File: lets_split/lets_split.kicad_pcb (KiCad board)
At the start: 2 copper layers, 112 x 79 mm, 62 parts, among them J1 3PIN, J2 6PIN, J3 3PIN, SW1 SW_PUSH, SW10 SW_PUSH, SW11 SW_PUSH, SW12 SW_PUSH, SW13 SW_PUSH, SW14 SW_PUSH, SW15 SW_PUSH, SW16 SW_PUSH, SW17 SW_PUSH, SW18 SW_PUSH, SW19 SW_PUSH, SW2 SW_PUSH, SW21 SW_PUSH, SW22 SW_PUSH, SW23 SW_PUSH, SW3 SW_PUSH, SW4 SW_PUSH, SW5 SW_PUSH, SW6 SW_PUSH, SW7 SW_PUSH, SW8 SW_PUSH, SW9 SW_PUSH, U2 HOLE, U3 HOLE, U4 HOLE, U5 HOLE

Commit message: added universal switch and stuff
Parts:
- removed ? (x2): SW_PUSH, flipalps:MXALPS_FLIP
- removed the G*** at (118.8, 78.0)
- removed the G*** at (127.0, 87.8)
- added G***: LOGO, Silks:AIRImicro, F.Cu at (141.0, 109.0)
- added G***: LOGO, Silks:BKB smaller chess, B.Cu at (62.0, 92.0)
- added G***: LOGO, Silks:Octopus1, F.Cu at (112.0, 92.0)
- added J10, J8, J9: Conn_01x01, BishopKicadConsolidated:PIN_1, F.Cu at (93.0, 122.1)
- added J11: Conn_01x01, BishopKicadConsolidated:PIN_1, F.Cu at (59.9, 35.7)
- added J12: Conn_01x01, BishopKicadConsolidated:PIN_1, F.Cu at (54.2, 51.0)
- added J4: Conn_01x01, BishopKicadConsolidated:PIN_1, F.Cu at (75.8, 37.9)
- added J5: Conn_01x01, BishopKicadConsolidated:PIN_1, F.Cu at (78.0, 37.9)
- added J6: Conn_01x01, BishopKicadConsolidated:PIN_1, F.Cu at (54.2, 53.6)
- added J7: Conn_01x01, BishopKicadConsolidated:PIN_1, F.Cu at (74.8, 48.4)
- added SW20: SW_PUSH, Universal-Switch-Footprint:MX-ALPs-PG1350-FLIP, F.Cu at (121.7, 104.0)
- added SW24: SW_PUSH, Universal-Switch-Footprint:MX-ALPs-PG1350-FLIP, F.Cu at (140.8, 104.0)
- added SW25: SW_PUSH, Universal-Switch-Footprint:MX-ALPs-PG1350-FLIP-2U, F.Cu at (131.2, 104.0)
- SW1, SW10, SW11, SW12, SW13, SW14, SW15, SW16, SW17, SW18, SW19, SW2, SW21, SW22, SW23, SW3, SW4, SW5, SW6, SW7, SW8, SW9: footprint flipalps:MXALPS_FLIP -> Universal-Switch-Footprint:MX-ALPs-PG1350-FLIP
- U1: value (none) -> TEENSY2.0
- moved D20 27.5 mm to (108.9, 94.5), turned to 180 degrees
- moved D5 18.9 mm to (69.7, 56.2)
- moved W1 12.1 mm to (131.2, 50.5)
- moved D21 11.3 mm to (147.2, 56.2), turned to 180 degrees
- moved D22 10.4 mm to (146.0, 75.4), turned to 180 degrees
- moved D23 10.3 mm to (147.3, 94.5), turned to 180 degrees
- moved D6 10.2 mm to (69.9, 75.4), turned to 180 degrees
- moved R1 9.85 mm to (93.1, 47.0), turned to 270 degrees
- moved R2 9.76 mm to (112.1, 47.0), turned to 90 degrees
- moved D17 8.66 mm to (125.4, 56.4), turned to 180 degrees
- moved D9 6.10 mm to (88.7, 56.4), turned to 180 degrees
- moved D13 5.63 mm to (108.3, 56.4), turned to 180 degrees
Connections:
- U1 pad 1: Net-(U1-Pad1) -> (no net)
- U1 pad 29: Net-(U1-Pad29) -> (no net)
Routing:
- net col5: track 133.7 -> 187.5 mm, vias 0 -> 1
- net VCC: track 27.2 -> 76.9 mm
- net col3: track 85.0 -> 123.0 mm, vias 0 -> 1
- net col2: track 68.2 -> 104.0 mm, vias 0 -> 1
- net col1: track 68.7 -> 99.0 mm
- net col4: track 112.3 -> 141.2 mm, vias 0 -> 1
- net data: track 117.5 -> 91.3 mm
- net GND: track 15.8 -> 42.0 mm, vias 0 -> 1
- net col0: track 96.5 -> 116.7 mm
- net Net-(D20-Pad2): track 8.15 -> 24.5 mm
- net Net-(D18-Pad2): track 6.11 -> 21.6 mm
- net xtradata: track 25.8 -> 10.8 mm
- net row3: track 143.1 -> 129.3 mm
- net Net-(D14-Pad2): track 6.62 -> 20.2 mm
- net Net-(D15-Pad2): track 6.65 -> 20.0 mm
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- added copper zone on B.Cu, net GND
- removed copper zone on B.Cu, net VCC
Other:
- outline, holes or cut-outs redrawn
- board text added: "Origonal design by Wootpatoot Update by Bishop Keyboards"
- board text added: "The standard English plural of octopus is octopuses."
- board text removed: "By Wootpatoot"

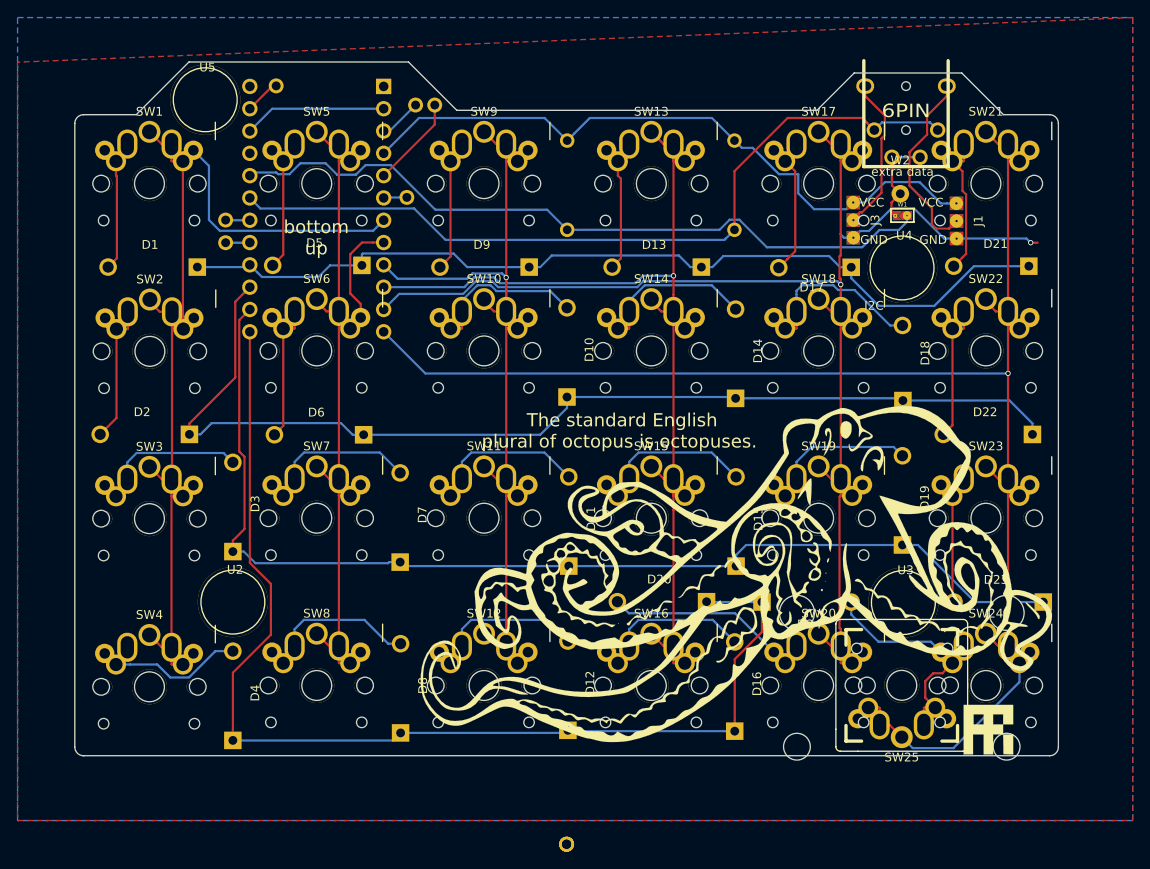
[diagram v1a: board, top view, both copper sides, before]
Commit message: fixed diodes broke traces
updated the diode footprint will have to fix traces now that the width of the diode pole spaces are different.
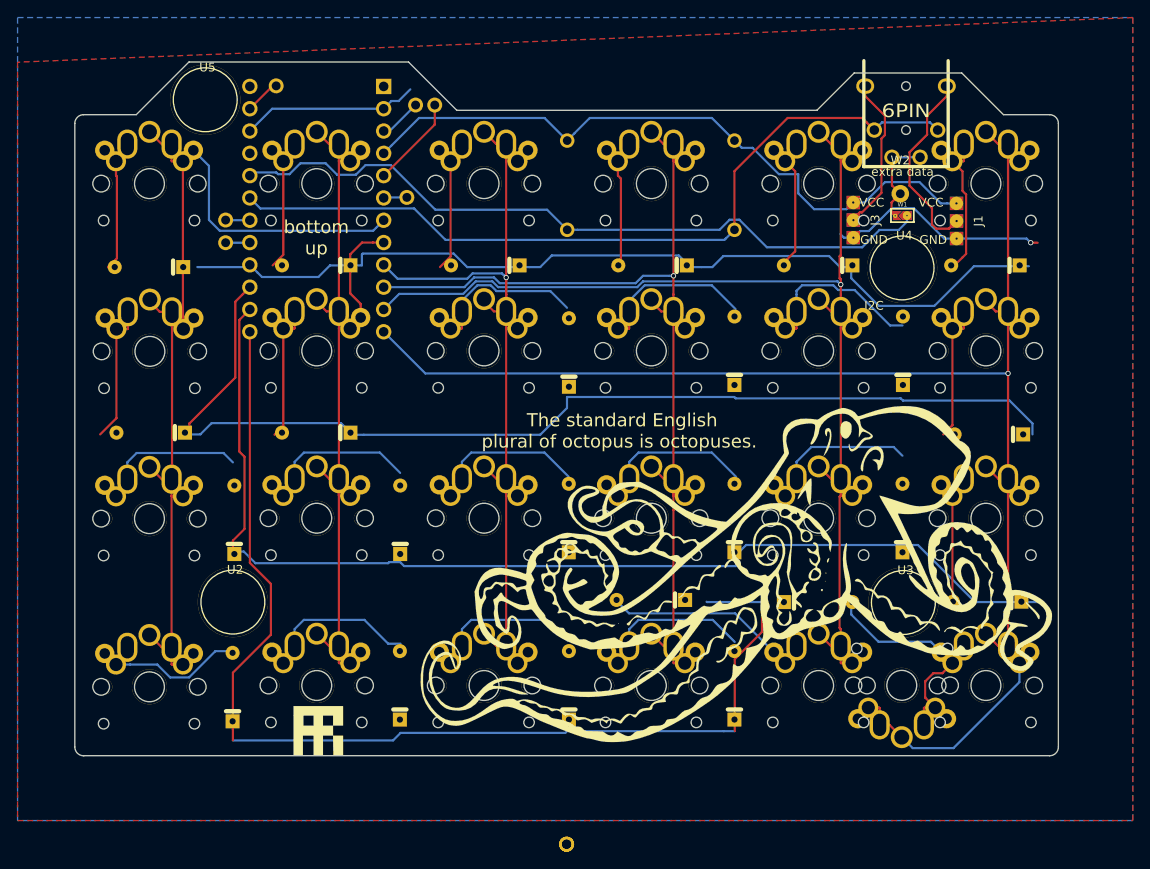
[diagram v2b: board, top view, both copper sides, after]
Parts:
- D1, D10, D11, D12, D13, D14, D15, D16, D17, D18, D19, D2, D20, D21, D22, D23, D24, D3, D4, D5, D6, D7, D8, D9: footprint Diodes_ThroughHole:Diode_DO-41_SOD81_Horizontal_RM10 -> BishopKicadConsolidated:D_axial_clean
- SW25: footprint Universal-Switch-Footprint:MX-ALPs-PG1350-FLIP-2U -> Universal-Switch-Footprint:MX-ALPs-PG1350-FLIP
- moved G*** 76.3 mm to (64.7, 109.1)
- moved D21 6.55 mm to (140.7, 56.2)
- moved D24 6.39 mm to (121.6, 94.5)
- moved D23 6.39 mm to (140.9, 94.5)
- moved D20 6.35 mm to (102.6, 94.3)
- moved D4 6.07 mm to (55.0, 104.2)
- moved D18 5.67 mm to (131.3, 65.9)
- moved D13 5.56 mm to (102.8, 56.2)
- moved D1 5.51 mm to (45.4, 56.4)
- moved D15 5.47 mm to (112.1, 84.9)
- moved D11 5.47 mm to (93.2, 84.9)
- moved D14 5.42 mm to (112.1, 65.9)
- moved D8 5.42 mm to (74.0, 104.0)
- moved D6 5.40 mm to (64.5, 75.2)
- moved D16 5.22 mm to (112.1, 104.0)
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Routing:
- net (no net): track 0.00 -> 279.6 mm
- net row1: track 121.7 -> 19.6 mm
- net row2: track 126.3 -> 28.9 mm
- net row0: track 104.4 -> 8.04 mm
- net Net-(D5-Pad2): track 16.6 -> 113.0 mm
- net row3: track 129.3 -> 49.3 mm
- net GND: track 42.0 -> 45.9 mm

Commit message: changed 3.5mm jack
updated 3.5mm jack to use the PJ320E
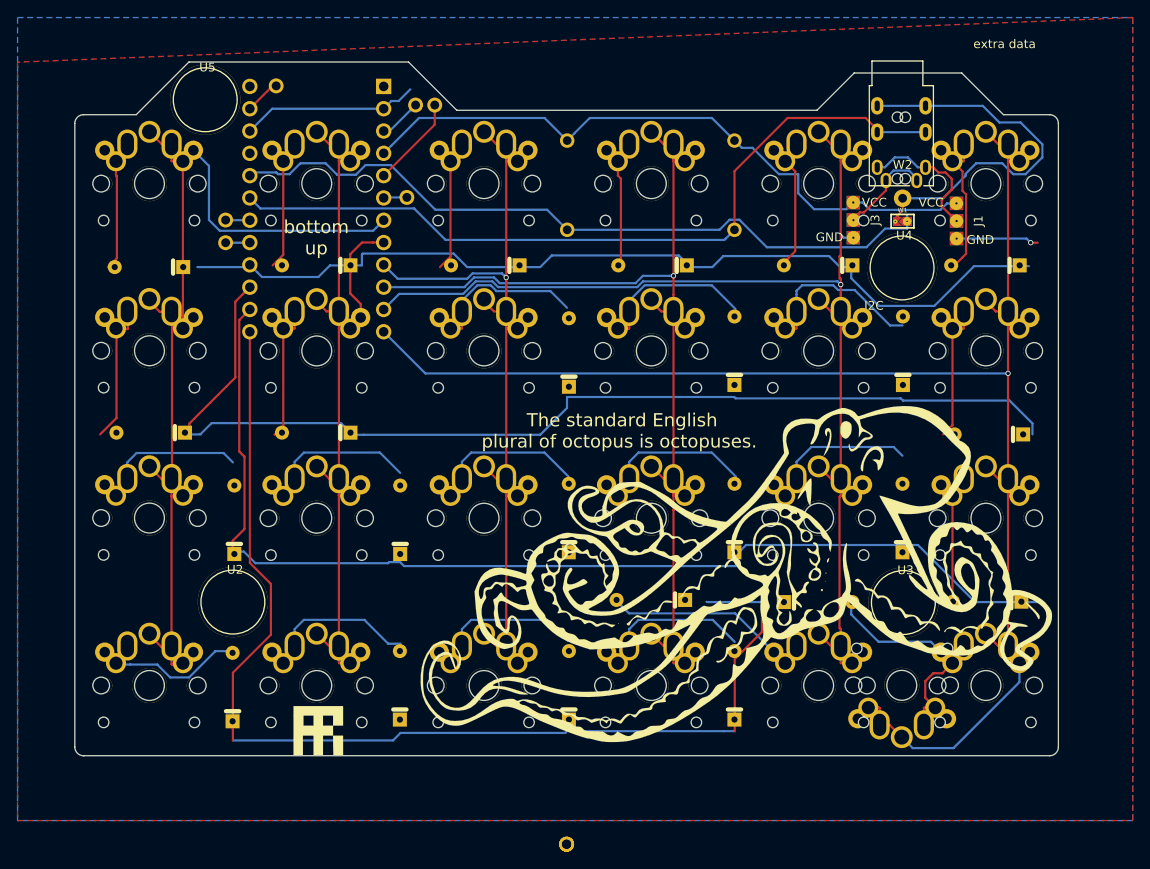
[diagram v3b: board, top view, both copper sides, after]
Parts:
- removed J2: 6PIN, footprint:4pin35mmAudio
- added TRRS1: 4pin 3.5mm, BishopKicadConsolidated:PJ320E_3.5mm_Jack_flip, F.Cu at (131.1, 39.3)
- moved W1 0.65 mm to (131.3, 51.1)
- moved W2 0.58 mm to (131.3, 48.5)
- moved SW4 0.15 mm to (45.5, 104.0)
- moved SW2 0.09 mm to (45.5, 65.9)
- moved SW3 0.07 mm to (45.5, 84.9)
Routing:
- net (no net): track 279.6 -> 64.0 mm
- net row1: track 19.6 -> 121.7 mm
- net row2: track 28.9 -> 126.3 mm
- net row0: track 8.04 -> 104.4 mm
- net Net-(D5-Pad2): track 113.0 -> 16.6 mm
- net xtradata: track 10.8 -> 44.8 mm
- net row3: track 49.3 -> 65.3 mm
- net GND: track 45.9 -> 31.3 mm
- net Net-(J3-Pad2): track 17.8 -> 11.1 mm
- net Net-(J1-Pad2): track 21.9 -> 15.9 mm
- net data: track 91.3 -> 89.4 mm
- net VCC: track 76.9 -> 75.6 mm
